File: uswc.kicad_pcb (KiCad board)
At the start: 4 copper layers, 54.5 x 38 mm, 68 parts, among them J1 USB_C_Receptacle_USB2.0_16P, J2 debug-port, J3 USB_B_Micro, J4 jlink, P1 DFP, SW1 DUT prot sel, SW2 orient sel, SW3 DUT prot sel, U1 FE1.1s, U10 SRV05-4, U2 W25Q32JVZP, U3 AT24CS01-STUM, U4 RP2040, U5 XC6206PxxxMR, U6 TXB0102DCU, U7 LM397, U8 ADG884xRM, U9 SRV05-4, Y1 12MHz 10ppm, Y2 12MHz 10ppm

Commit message: fab jingtuo
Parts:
- added R18: 4.7k, Resistor_SMD:R_0603_1608Metric, F.Cu at (91.5, 117.6)
- added R19: 4.7k, Resistor_SMD:R_0603_1608Metric, F.Cu at (99.7, 111.1)
- added TP5: VBUS, TestPoint:TestPoint_THTPad_D1.5mm_Drill0.7mm, F.Cu at (99.4, 104.5)
- added TP6: GND, TestPoint:TestPoint_Bridge_Pitch2.0mm_Drill0.7mm, F.Cu at (97.3, 101.8)
- added TP7: 3V3, TestPoint:TestPoint_THTPad_D1.5mm_Drill0.7mm, F.Cu at (76.0, 113.0)
- FB1: footprint Inductor_SMD_Wurth:L_Wurth_WE-LQSH-2512 -> Inductor_SMD:L_0805_2012Metric
- J3: value USB_B_Micro -> USB3150-30-130-A
- moved FB1 42.7 mm to (56.7, 127.2), turned to 180 degrees
- moved TP1 1.12 mm to (101.2, 108.9)
- moved TP3 1.00 mm to (96.2, 106.6)
- moved U6 0.20 mm to (66.4, 126.9)
- moved R5 0.10 mm to (91.5, 116.1)
- moved U9 0.10 mm to (95.1, 119.0)
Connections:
- net Net-(U1-LED1/EESCL) renamed SCL
- net Net-(U1-TESTJ/EESDA) renamed SDA
- J3 pad 4: GND -> unconnected-(J3-ID-Pad4)
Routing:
- net GND: track 73.6 -> 82.2 mm, vias 43 -> 42
- net SHIELD: track 100.1 -> 95.7 mm, vias 0 -> 2
- net HUB_3V3: track 24.8 -> 27.5 mm
- net SDA: track 15.0 -> 16.5 mm
- net Net-(U3-WP): track 4.75 -> 5.79 mm
- net JLK_D-: track 13.3 -> 12.8 mm
- net +3V3: vias 15 -> 13
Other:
- board text added: "JLCJLCJLCJLC"
- board text added: "v0.1"
- board text removed: "expm 1"

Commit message: fab 8012
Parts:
- P1: footprint lib:jingtuojin_918-118A2021S40000 -> lib:GT-USB-8012A
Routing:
- net GND: track 82.2 -> 82.7 mm
- net VBUS: track 39.7 -> 40.2 mm

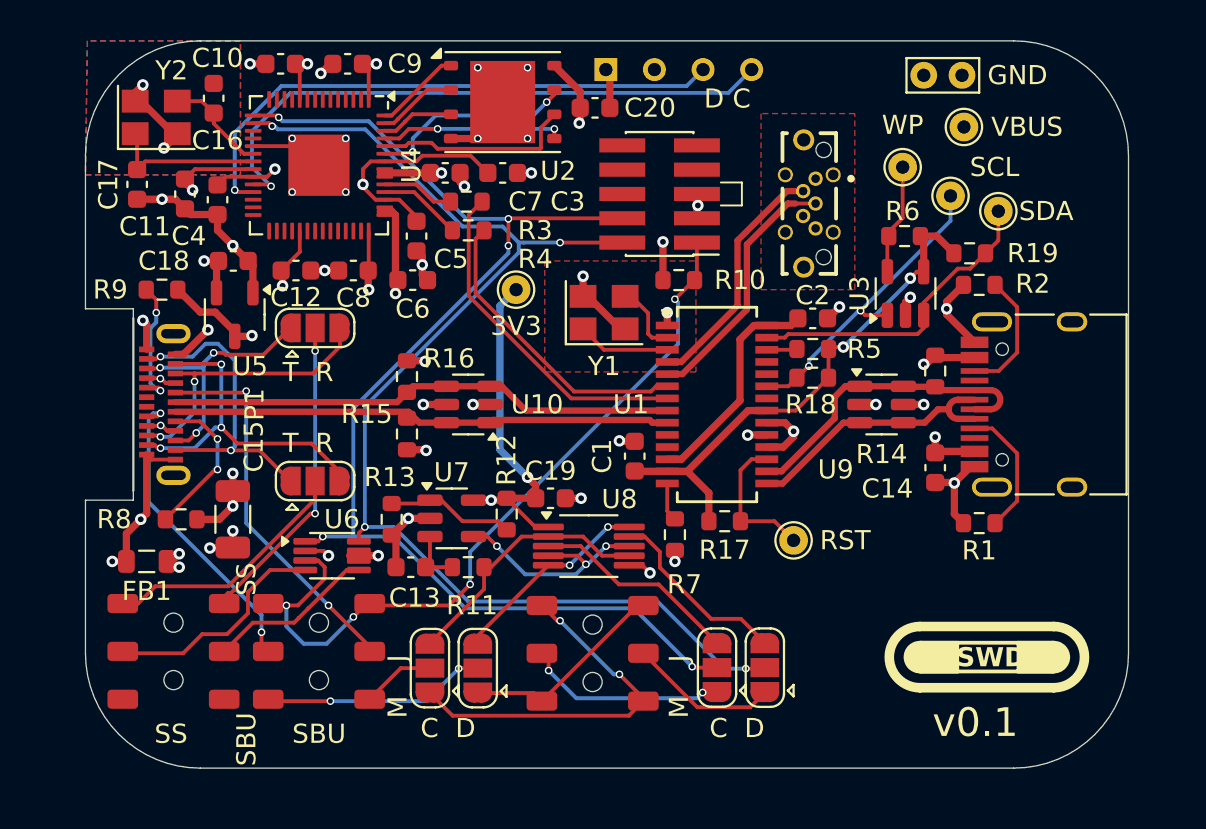
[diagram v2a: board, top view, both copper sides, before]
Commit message: 2 layer, analog switches
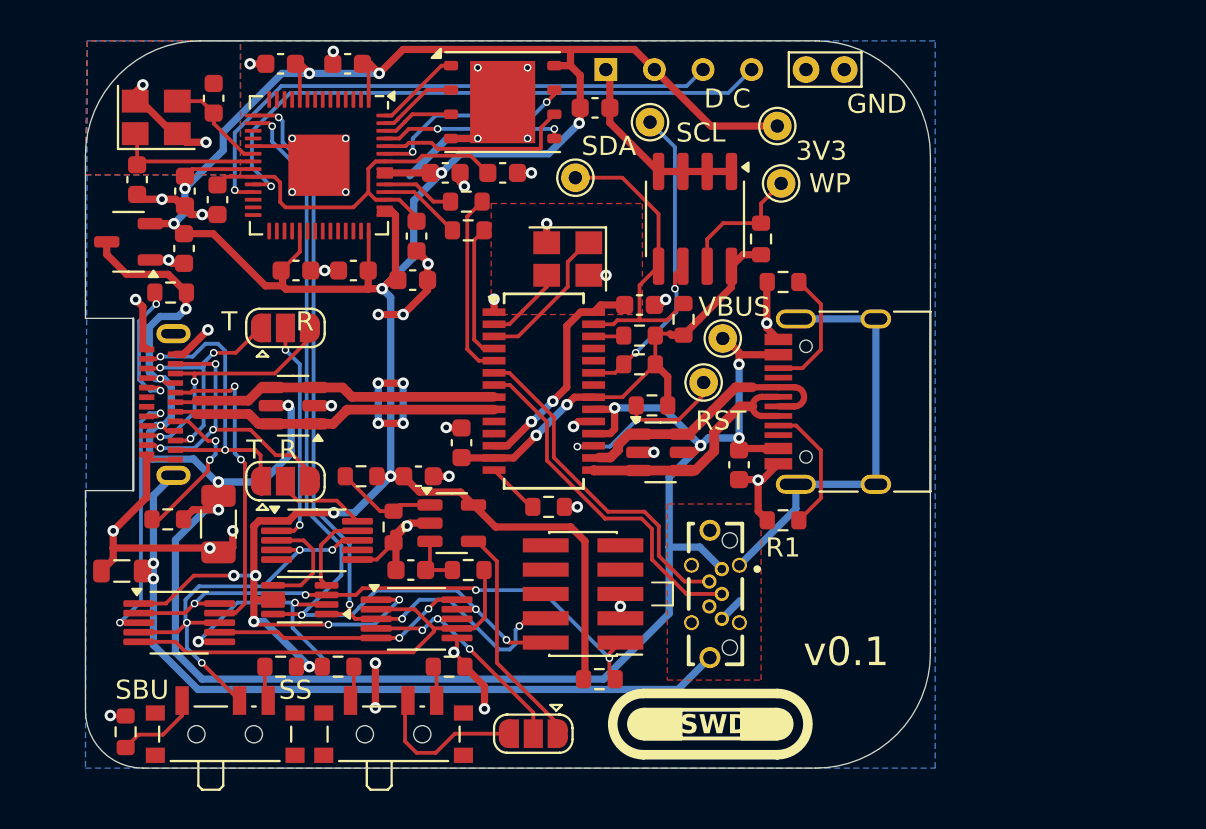
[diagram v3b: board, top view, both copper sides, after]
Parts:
- removed JP4: OMsel C I, Jumper:SolderJumper-3_P1.3mm_Open_RoundedPad1.0x1.5mm
- removed JP5: OMsel D O, Jumper:SolderJumper-3_P1.3mm_Open_RoundedPad1.0x1.5mm
- removed JP6: OMsel D I, Jumper:SolderJumper-3_P1.3mm_Open_RoundedPad1.0x1.5mm
- removed R14: 1.5k, Resistor_SMD:R_0603_1608Metric
- removed R15, R16: 15k, Resistor_SMD:R_0603_1608Metric
- removed SW3: DUT prot sel, lib:K3-1390S-D1
- added R20: 5.1k, Resistor_SMD:R_0603_1608Metric, F.Cu at (66.7, 132.7)
- added R21: 5.1k, Resistor_SMD:R_0603_1608Metric, F.Cu at (72.5, 132.7)
- added R22: 5.1k, Resistor_SMD:R_0603_1608Metric, F.Cu at (63.7, 132.7)
- added R23: 5.1k, Resistor_SMD:R_0603_1608Metric, F.Cu at (55.6, 136.1)
- added U11: ADG884xRM, Package_SO:MSOP-10_3x3mm_P0.5mm, F.Cu at (65.6, 126.1)
- added U12: ADG884xRM, Package_SO:MSOP-10_3x3mm_P0.5mm, F.Cu at (58.4, 130.4)
- JP3: value OMsel C O -> OMsel
- SW1: value DUT prot sel -> SW_SPDT; footprint lib:K3-1390S-D1 -> Button_Switch_SMD:SW_SPDT_PCM12
- SW2: value orient sel -> SW_SPDT; footprint lib:K3-1390S-D1 -> Button_Switch_SMD:SW_SPDT_PCM12
- U3: value AT24CS01-STUM -> AT24CS02-SSHM; footprint Package_TO_SOT_SMD:SOT-23-5 -> Package_SO:SOIC-8_3.9x4.9mm_P1.27mm
- moved TP1 22.2 mm to (79.1, 107.2)
- moved J4 21.3 mm to (79.5, 128.9)
- moved R10 21.3 mm to (80.3, 133.3)
- moved J3 21.0 mm to (86.1, 128.9)
- moved TP5 16.8 mm to (86.8, 115.5)
- moved TP2 16.2 mm to (83.0, 104.2)
- moved TP7 16.1 mm to (89.7, 104.5)
- moved R19 15.3 mm to (84.8, 114.5), turned to -90 degrees
- moved U9 11.8 mm to (83.5, 121.5)
- moved U3 11.7 mm to (85.3, 109.3), turned to -90 degrees
- moved SW2 11.1 mm to (69.6, 135.9), turned to 0 degrees
- moved C14 10.3 mm to (87.7, 122.2)
- moved J1 10.3 mm to (93.8, 118.8)
- moved R1 10.3 mm to (90.0, 125.0)
- moved R2 10.3 mm to (90.0, 112.6)
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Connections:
- JP3 pad 1: DUT_SWC/D_M -> Net-(JP3-A)
- JP3 pad 2: DUT_SWC/D_SBU -> Net-(JP3-C)
- JP3 pad 3: DUT_SWC/D_J -> Net-(JP3-B)
- R11 pad 2: DUT_SWC/D_J -> DUT_SWC/D_SBU
- SW1 pad 1: DUT_VREF -> Net-(SW1-A)
- SW1 pad 2: DUT_SBU2 -> PROT_SEL
- SW1 pad 3: DUT_SWD/C_SBU -> Net-(SW1-C)
- SW2 pad 1: DUT_SWC/D_M -> Net-(SW2-A)
- SW2 pad 2: DUT_SWC_M -> Net-(JP3-B)
- SW2 pad 3: DUT_SWD/C_M -> Net-(SW2-C)
- U1 pad 4: JLK_D- -> DAP_D-
- U1 pad 5: JLK_D+ -> DAP_D+
- U1 pad 6: DAP_D- -> JLK_D-
- U1 pad 7: DAP_D+ -> JLK_D+
- U3 pad 1: SCL -> GND
- U3 pad 3: SDA -> GND
- U3 pad 4: HUB_3V3 -> GND
- U3 pad 5: Net-(U3-WP) -> SDA
- U7 pad 4: Net-(U8-IN1) -> Net-(JP3-A)
- U8 pad 10: DUT_SWD/C_J -> DUT_SWD/C_SBU
- U8 pad 2: DUT_SWC/D_J -> DUT_SWC/D_SBU
- U8 pad 3: DUT_SWC_J -> DUT_SWC
- U8 pad 4: Net-(U8-IN1) -> Net-(JP3-C)
- U8 pad 5: DUT_SWD/C_J -> DUT_SWD/C_SBU
- U8 pad 7: DUT_SWC/D_J -> DUT_SWC/D_SBU
- U8 pad 8: Net-(U8-IN1) -> Net-(JP3-C)
- U8 pad 9: DUT_SWD_J -> DUT_SWD
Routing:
- net +3V3: track 59.1 -> 163.1 mm, vias 13 -> 15
- net VBUS: track 40.2 -> 108.3 mm
- net GND: track 82.7 -> 119.5 mm, vias 42 -> 51
- net SHIELD: track 95.8 -> 63.6 mm
- net PROT_SEL: track 0.00 -> 23.0 mm, vias 0 -> 4
- net DUT_SWC: track 65.9 -> 43.1 mm, vias 5 -> 4
- net DUT_SWC/D_SBU: track 3.82 -> 25.2 mm
- net DUT_SWC/D_M: track 19.4 -> 0.00 mm, vias 2 -> 0
- net DUT_SWD: track 64.9 -> 45.9 mm
- net DUT_SWC/D_J: track 13.8 -> 0.00 mm
- net Net-(JP3-C): track 0.00 -> 12.8 mm, vias 0 -> 3
- net Net-(JP3-A): track 0.00 -> 12.5 mm
- net Net-(U8-IN1): track 11.7 -> 0.00 mm, vias 3 -> 0
- net DUT_SWC_J: track 10.9 -> 0.00 mm
- net DUT_SWD/C_M: track 10.9 -> 0.00 mm
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- removed copper zone on In2.Cu, net +3V3
- removed copper zone on In1.Cu, net GND
- removed copper zone on In2.Cu, net GND
- removed copper zone on In2.Cu, net VBUS
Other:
- board size 54.5 x 38 mm -> 44.2 x 38 mm
- copper layers 4 -> 2
- board text removed: "C D"
- board text removed: "M J"

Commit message: pre level shifter
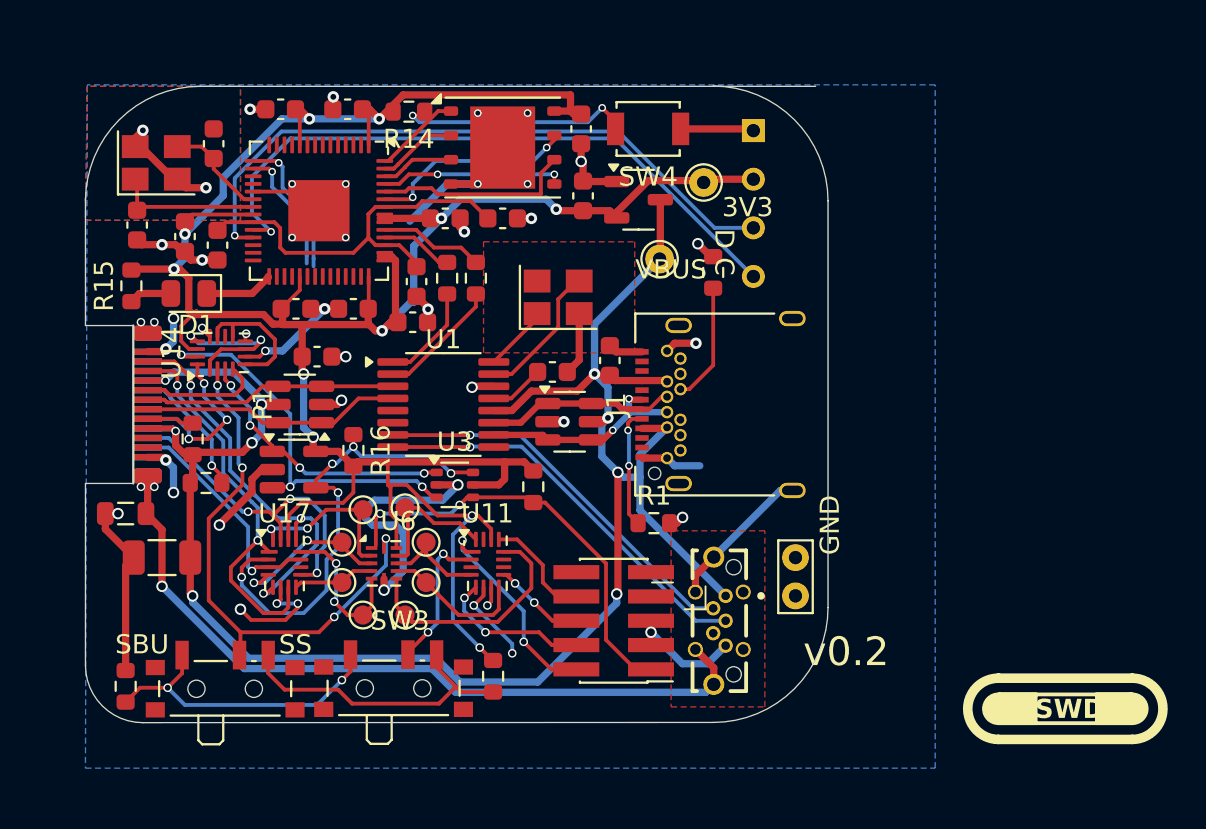
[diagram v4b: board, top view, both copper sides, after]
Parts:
- removed C13: 1uF, Capacitor_SMD:C_0603_1608Metric
- removed C2: 10uF, Capacitor_SMD:C_0603_1608Metric
- removed JP1: T/RX C, Jumper:SolderJumper-3_P1.3mm_Open_RoundedPad1.0x1.5mm
- removed JP2: T/RX D, Jumper:SolderJumper-3_P1.3mm_Open_RoundedPad1.0x1.5mm
- removed JP3: OMsel, Jumper:SolderJumper-3_P1.3mm_Open_RoundedPad1.0x1.5mm
- removed R11, R12, R13, R17, R5, R6: 100k, Resistor_SMD:R_0603_1608Metric
- removed R18, R19: 4.7k, Resistor_SMD:R_0603_1608Metric
- removed R20, R21: 5.1k, Resistor_SMD:R_0603_1608Metric
- removed R7: 2.7k 1%, Resistor_SMD:R_0603_1608Metric
- removed SW2: SW_SPDT, Button_Switch_SMD:SW_SPDT_PCM12
- removed U12, U8: ADG884xRM, Package_SO:MSOP-10_3x3mm_P0.5mm
- added D1: LED, LED_SMD:LED_0805_2012Metric, F.Cu at (58.9, 113.2)
- added R14: 56k, Resistor_SMD:R_0603_1608Metric, F.Cu at (70.4, 103.7)
- added R15: 1k, Resistor_SMD:R_0603_1608Metric, F.Cu at (55.9, 112.8)
- added R16: 56k, Resistor_SMD:R_0603_1608Metric, F.Cu at (67.5, 121.4)
- added SW3: SW_SPDT, Button_Switch_SMD:SW_SPDT_PCM12, F.Cu at (69.6, 133.5)
- added SW4: SW_Push, Button_Switch_SMD:SW_SPST_B3U-1000P, F.Cu at (82.9, 104.6)
- added TP10: inline, TestPoint:TestPoint_Pad_D1.0mm, F.Cu at (66.9, 126.2)
- added TP11: inline, TestPoint:TestPoint_Pad_D1.0mm, F.Cu at (68.0, 124.5)
- added TP8: inline, TestPoint:TestPoint_Pad_D1.0mm, F.Cu at (68.0, 130.0)
- added TP9: inline, TestPoint:TestPoint_Pad_D1.0mm, F.Cu at (66.9, 128.3)
- added U14: ~, Package_DFN_QFN:UQFN-16_1.8x2.6mm_P0.4mm, F.Cu at (60.6, 116.3)
- added U17: ~, Package_DFN_QFN:UQFN-16_1.8x2.6mm_P0.4mm, F.Cu at (63.9, 127.3)
- C1: value 10uF -> 1uF
- J1: value USB_C_Receptacle_USB2.0_16P -> USB_C_Receptacle; footprint Connector_USB:USB_C_Receptacle_HRO_TYPE-C-31-M-12 -> Connector_USB:USB_C_Receptacle_Amphenol_12401548E4-2A
- P1: footprint lib:GT-USB-8012A -> lib:jingtuojin_918-118A2021Y40005
- R10: value 100k -> 56k
- TP1: value SDA -> inline; footprint TestPoint:TestPoint_THTPad_D1.5mm_Drill0.7mm -> TestPoint:TestPoint_Pad_D1.0mm
- TP2: value SCL -> inline; footprint TestPoint:TestPoint_THTPad_D1.5mm_Drill0.7mm -> TestPoint:TestPoint_Pad_D1.0mm
- TP3: value WP -> inline; footprint TestPoint:TestPoint_THTPad_D1.5mm_Drill0.7mm -> TestPoint:TestPoint_Pad_D1.0mm
- TP4: value RST -> inline; footprint TestPoint:TestPoint_THTPad_D1.5mm_Drill0.7mm -> TestPoint:TestPoint_Pad_D1.0mm
- U1: value FE1.1s -> ~; footprint Package_SO:SSOP-28_3.9x9.9mm_P0.635mm -> Package_SO:QSOP-16_3.9x4.9mm_P0.635mm
- U11: value ADG884xRM -> ~; footprint Package_SO:MSOP-10_3x3mm_P0.5mm -> Package_DFN_QFN:UQFN-16_1.8x2.6mm_P0.4mm
- U3: value AT24CS02-SSHM -> 74LVC1G3157; footprint Package_SO:SOIC-8_3.9x4.9mm_P1.27mm -> Package_TO_SOT_SMD:SOT-363_SC-70-6
- U6: value TXB0102DCU -> TXB0104RUT; footprint Package_SO:VSSOP-8_2.3x2mm_P0.5mm -> Package_DFN_QFN:Texas_R-PUQFN-N12
- moved TP3 27.9 mm to (71.3, 128.3)
- moved TP6 27.5 mm to (90.6, 129.0), turned to 90 degrees
- moved U5 26.7 mm to (82.4, 108.3), turned to 0 degrees
- moved TP2 24.9 mm to (71.3, 126.2)
- moved C18 21.0 mm to (79.5, 108.1), turned to 90 degrees
- moved TP4 19.8 mm to (70.2, 130.0)
- moved TP1 19.4 mm to (70.2, 124.4)
- moved U3 18.7 mm to (72.8, 123.2), turned to 0 degrees
- moved R22 11.1 mm to (74.8, 133.2), turned to -90 degrees
- moved R10 10.6 mm to (76.9, 123.3), turned to 90 degrees
- moved R9 10.1 mm to (59.8, 123.1), turned to 180 degrees
- moved U11 8.98 mm to (74.5, 127.3)
- moved U7 8.70 mm to (64.4, 122.4)
- moved C14 8.68 mm to (80.9, 116.7), turned to 90 degrees
- moved C19 8.19 mm to (65.6, 116.5)
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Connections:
- net Net-(U2-~{CS}) renamed BOOT
- C1 pad 1: HUB_3V3 -> GND
- C1 pad 2: GND -> Net-(U1-VDD33)
- J4 pad 2: DUT_SWD -> DUT_SWD/TMS_J
- J4 pad 4: DUT_SWC -> DUT_SWC/TCK_J
- J4 pad 6: unconnected-(J4-SWO-Pad6) -> DUT_SWO/TDO_J
- J4 pad 8: unconnected-(J4-TDI-Pad8) -> DUT_TDI_J
- P1 pad A10: Net-(JP2-B) -> SS_A10
- P1 pad A11: Net-(JP1-B) -> SS_A11
- P1 pad A2: Net-(JP1-A) -> unconnected-(P1-TX1+-PadA2)
- P1 pad A3: Net-(JP2-A) -> unconnected-(P1-TX1--PadA3)
- P1 pad A8: DUT_SBU1 -> DUT_SBU_A
- P1 pad B10: Net-(JP2-B) -> SS_B10
- P1 pad B11: Net-(JP1-B) -> SS_B11
- P1 pad B2: Net-(JP1-A) -> unconnected-(P1-TX2+-PadB2)
- P1 pad B3: Net-(JP2-A) -> unconnected-(P1-TX2--PadB3)
- P1 pad B8: DUT_SBU2 -> DUT_SBU_B
- SW1 pad 2: PROT_SEL -> USE_SS
- TP1 pad 1: SDA -> /DUT_SWD/TMS
- TP2 pad 1: SCL -> /DUT_SWC/TCK
- TP3 pad 1: Net-(U3-WP) -> /DUT_SWO/TDO
- TP4 pad 1: Net-(U1-~{XRSTJ}) -> /DUT_TDI
- U1 pad 1: GND -> DAP_D-
- U1 pad 10: unconnected-(U1-DM1-Pad10) -> D-
- U1 pad 11: unconnected-(U1-DP1-Pad11) -> D+
- U1 pad 12: HUB_1V8 -> VBUS
- U1 pad 13: HUB_3V3 -> Net-(U1-VDD33)
- U1 pad 14: Net-(U1-REXT) -> GND
- U1 pad 15: D- -> Net-(U1-XO)
- U1 pad 16: D+ -> Net-(U1-XI)
- U1 pad 2: Net-(U1-XOUT) -> DAP_D+
- U1 pad 3: Net-(U1-XIN) -> DUT_D-
- U1 pad 4: DAP_D- -> DUT_D+
- U1 pad 5: DAP_D+ -> unconnected-(U1-DM2--Pad5)
- U1 pad 6: JLK_D- -> unconnected-(U1-DP2+-Pad6)
- U1 pad 7: JLK_D+ -> JLK_D-
- U1 pad 8: DUT_D- -> JLK_D+
- U1 pad 9: DUT_D+ -> unconnected-(U1-~{RESET}/CDP-Pad9)
- U11 pad 1: +3V3 -> DUT_SWD/TMS_J
- U11 pad 10: DUT_SS_C -> unconnected-(U11-NC-Pad10)
- U11 pad 2: DUT_SS_D -> USE_PICO
- U11 pad 3: DUT_SWD/C_SS -> DUT_SWC/TCK_P
- U11 pad 4: PROT_SEL -> /DUT_SWC/TCK
- U11 pad 5: unconnected-(U11-S1B-Pad5) -> DUT_SWC/TCK_J
- U11 pad 7: unconnected-(U11-S2B-Pad7) -> DUT_SWO/TDO_P
- U11 pad 8: PROT_SEL -> /DUT_SWO/TDO
- U11 pad 9: DUT_SWC/D_SS -> DUT_SWO/TDO_J
- U3 pad 1: GND -> DUT_VREF_A
- U3 pad 3: GND -> DUT_VREF_B
- U3 pad 4: GND -> DUT_VREF
- U3 pad 5: SDA -> +3V3
- U3 pad 6: SCL -> SS_DIR
- U4 pad 15: DUT_SWC -> DUT_SWC/TCK_P
- U4 pad 16: DUT_SWD -> DUT_SWD/TMS_P
- U4 pad 17: DUT_SWD_IN -> DUT_SWO/TDO_P
- U4 pad 18: unconnected-(U4-GPIO15-Pad18) -> DUT_TDI_P
- U4 pad 29: unconnected-(U4-GPIO18-Pad29) -> Net-(D1-K)
- U6 pad 1: DUT_SWC -> DUT_VREF
- U6 pad 2: GND -> /SS_B10_NORM
- U6 pad 3: DUT_VREF -> /SS_B11_NORM
- U6 pad 4: DUT_SWC/D_SS -> /SS_A10_NORM
- U6 pad 5: DUT_SWD/C_SS -> /SS_A11_NORM
- U6 pad 6: +3V3 -> GND
- U6 pad 7: +3V3 -> /DUT_TDI
- U6 pad 8: DUT_SWD -> /DUT_SWO/TDO
- U7 pad 1: Net-(U7--) -> DUT_VREF_A
- U7 pad 3: Net-(U7-+) -> DUT_VREF_B
- U7 pad 4: Net-(JP3-A) -> SS_DIR
- Y1 pad 1: Net-(U1-XIN) -> Net-(U1-XI)
- Y1 pad 3: Net-(U1-XOUT) -> Net-(U1-XO)
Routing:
- net DUT_SWD: track 45.9 -> 0.00 mm, vias 4 -> 0
- net DUT_SWC: track 43.1 -> 0.00 mm, vias 4 -> 0
- net USE_SS: track 0.00 -> 27.9 mm, vias 0 -> 4
- net SS_DIR: track 0.00 -> 25.2 mm, vias 0 -> 5
- net HUB_3V3: track 24.0 -> 0.00 mm, vias 2 -> 0
- net PROT_SEL: track 23.0 -> 0.00 mm, vias 4 -> 0
- net DUT_VREF_B: track 0.00 -> 20.8 mm, vias 0 -> 3
- net SS_A11: track 0.00 -> 20.8 mm, vias 0 -> 3
- net SS_A10: track 0.00 -> 20.5 mm, vias 0 -> 2
- net +3V3: track 163.1 -> 144.9 mm, vias 15 -> 11
- net SCL: track 17.5 -> 0.00 mm, vias 2 -> 0
- net DUT_SWC/D_SBU: track 25.2 -> 7.96 mm, vias 0 -> 2
- net SS_B10: track 0.00 -> 17.1 mm, vias 0 -> 3
- net DUT_SBU1: track 16.3 -> 0.00 mm, vias 2 -> 0
- net SDA: track 16.2 -> 0.00 mm
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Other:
- board size 44.2 x 38 mm -> 38.8 x 33.3 mm
- board text added: "v0.2"
- board text removed: "T R"
- board text removed: "v0.1"
